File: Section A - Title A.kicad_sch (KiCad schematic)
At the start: 0 parts

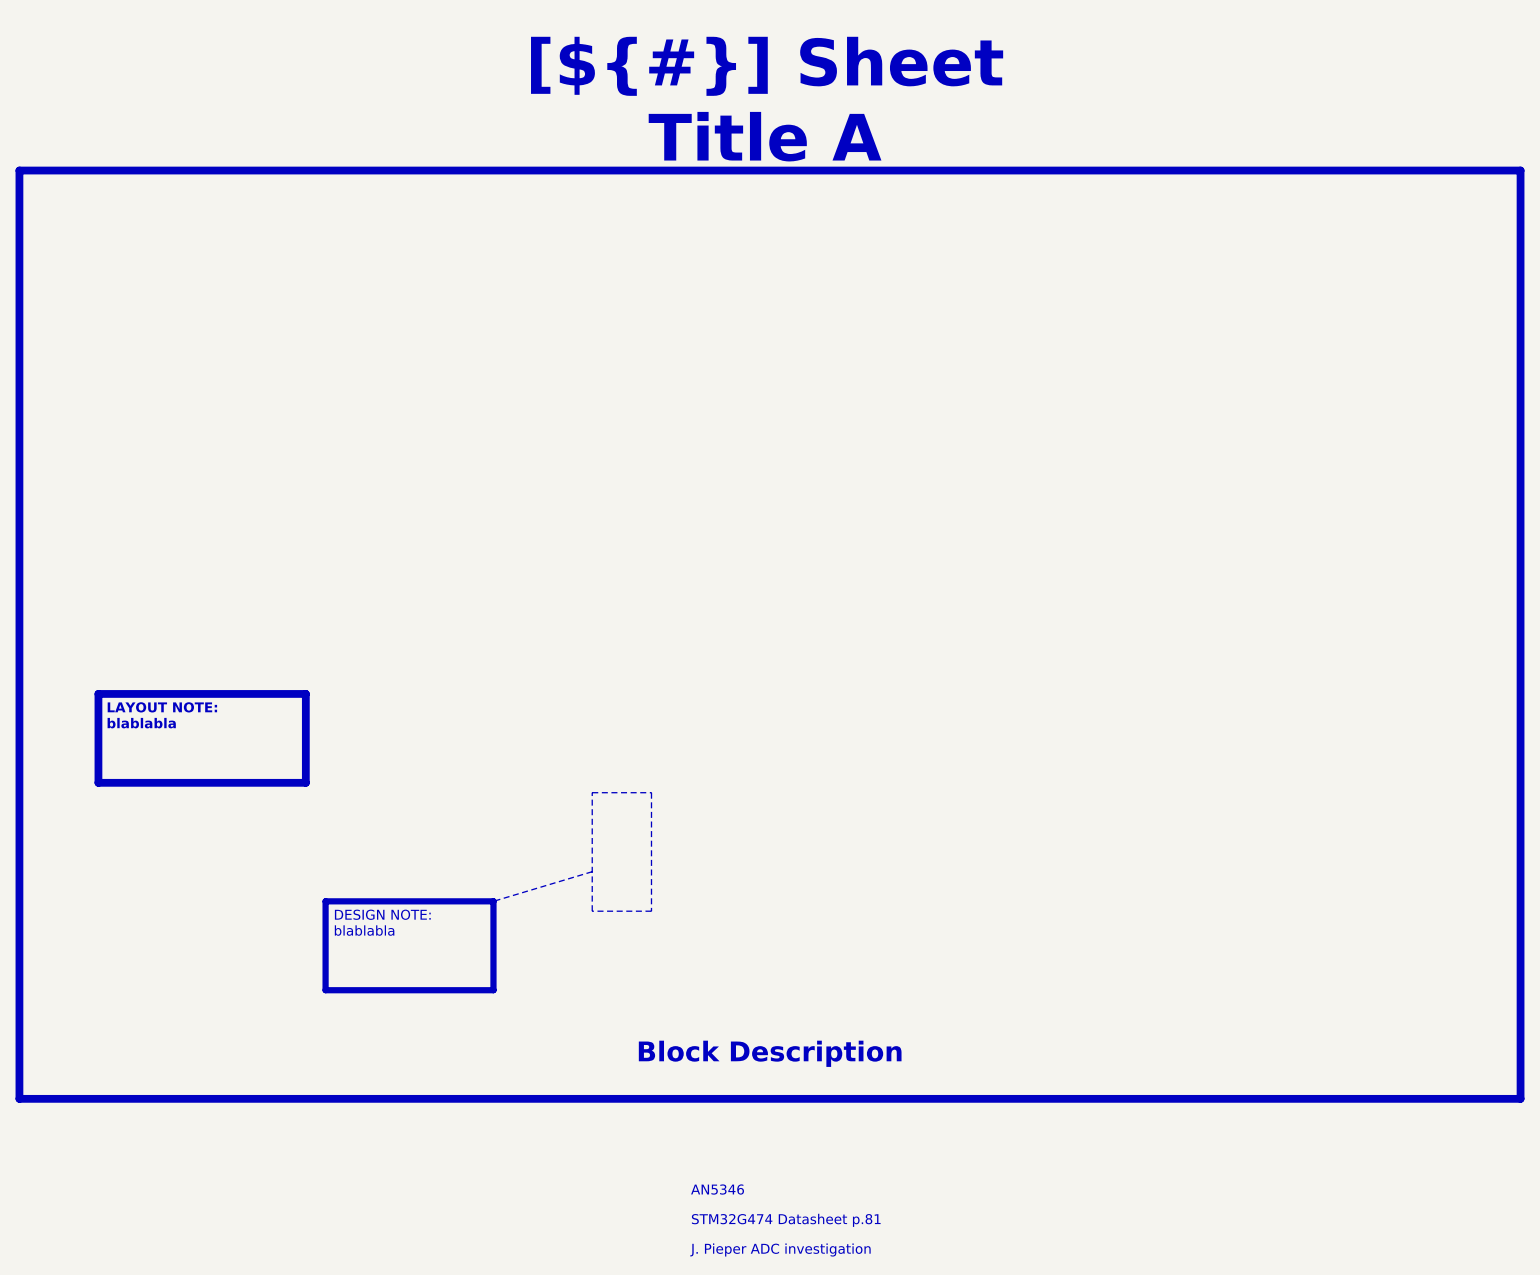
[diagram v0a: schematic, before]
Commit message: Save KiCad 10 design work
Snapshot of the schematic and PCB work done since the initial template
commit: AD7606C-18 ADC, 3x INA241A2 + PBV 1 mOhm shunts, MR60PW phase
connectors, LT8362 boost and LT3045-1 / LTC6655 analog supplies, project
libraries (lib/) and their sym/fp-lib-table.

.gitignore now excludes local history, SpinRender working files, the
stray .step export and Component Search Engine download leftovers.

Co-Authored-By: Claude Opus 5.5 <noreply@anthropic.com>
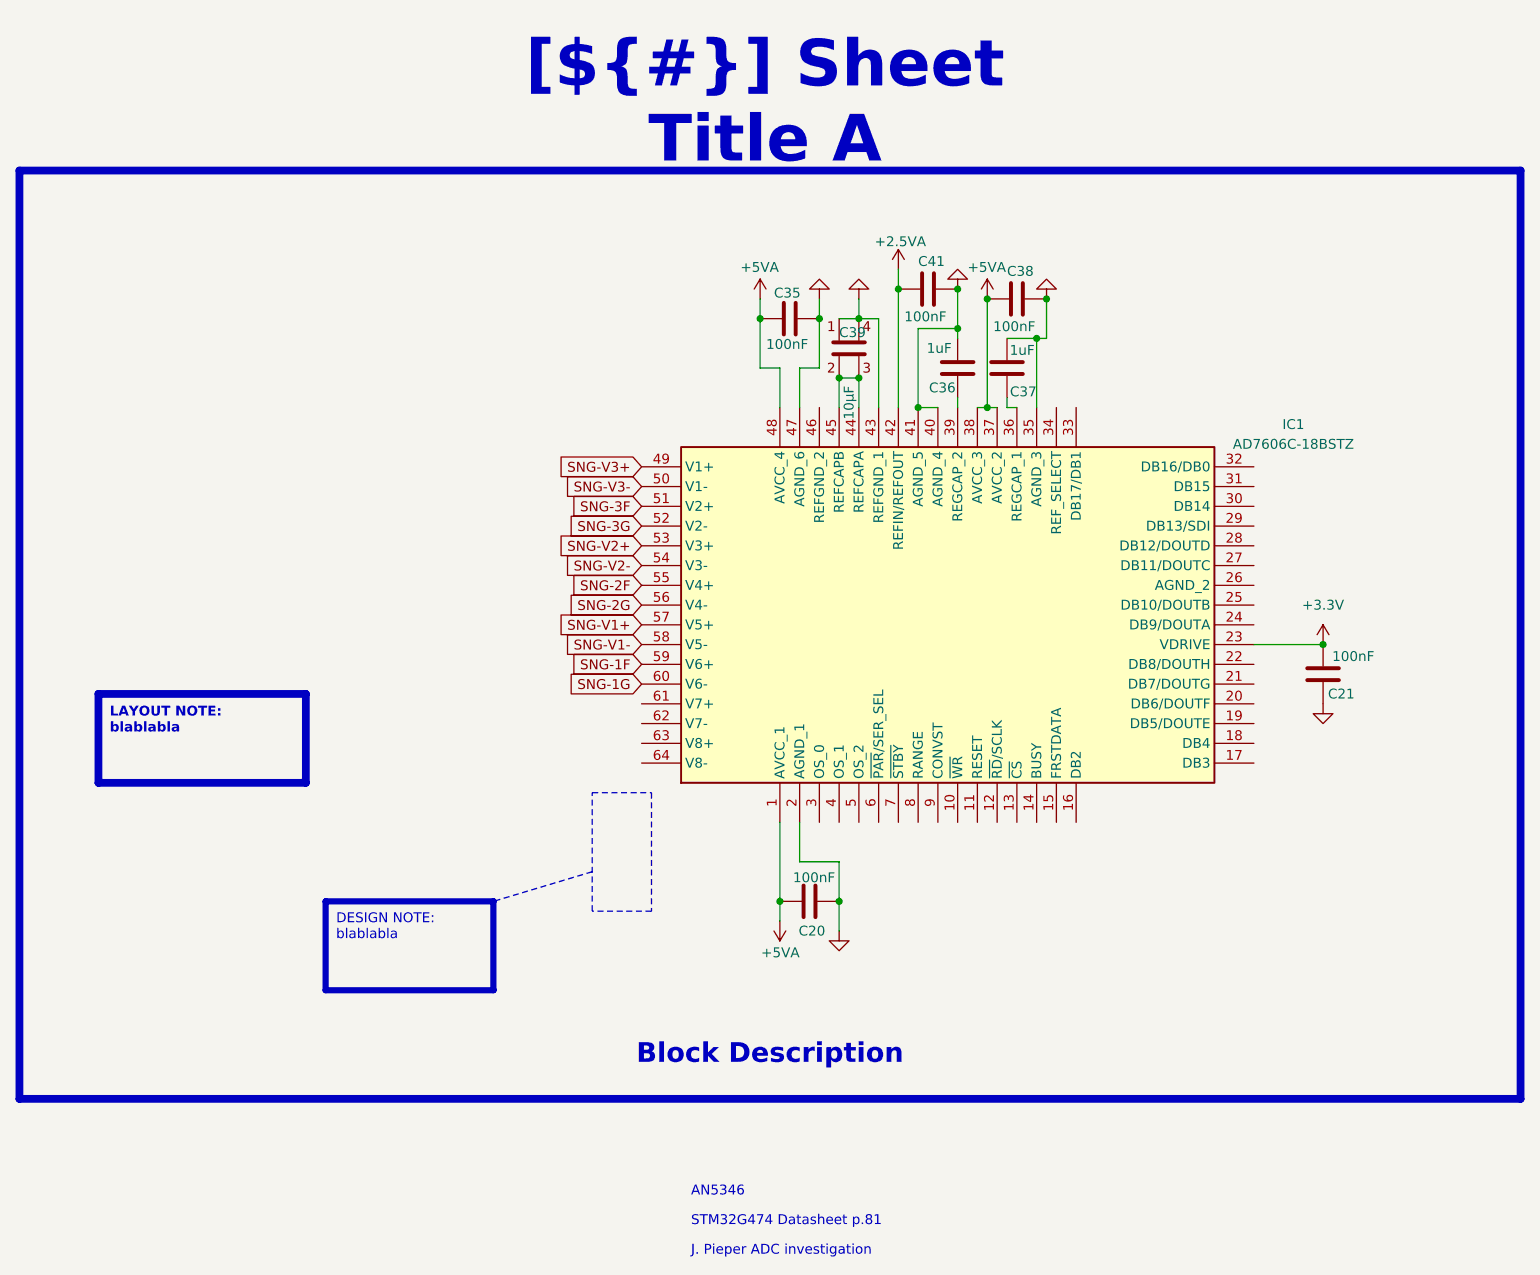
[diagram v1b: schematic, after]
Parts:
- added C20, C21, C35, C38, C41: 100nF, Capacitor_SMD:C_0603_1608Metric, symbol Device:C
- added C36, C37: 1uF, Capacitor_SMD:C_0603_1608Metric, symbol Device:C
- added C39: 10µF, Capacitor_SMD:C_0805_2012Metric, symbol Device:C
- added IC1: AD7606C-18BSTZ, QFP50P1200X1200X160-64N, symbol AD7606C-18BSTZ:AD7606C-18BSTZ
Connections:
- new net: C37.1, IC1.36 (REGCAP_1)
- new net: C36.1, IC1.39 (REGCAP_2)
- new net: C39.2, C39.3, IC1.44 (REFCAPA), IC1.45 (REFCAPB)
- new net +2.5VA: C41.2, IC1.42 (REFIN/REFOUT)
- new net +3.3V: C21.2, IC1.23 (VDRIVE)
- new net +5VA: C20.1, C35.2, C38.2, IC1.1 (AVCC_1), IC1.37 (AVCC_2), IC1.38 (AVCC_3), IC1.48 (AVCC_4)
- new net GND: C20.2, C21.1, C35.1, C36.2, C37.2, C38.1, C39.1, C39.4, C41.1, IC1.2 (AGND_1), IC1.35 (AGND_3), IC1.40 (AGND_4), IC1.41 (AGND_5), IC1.43 (REFGND_1), IC1.47 (AGND_6)
- new net SNG-1F: IC1.59 (V6+)
- new net SNG-1G: IC1.60 (V6-)
- new net SNG-2F: IC1.55 (V4+)
- new net SNG-2G: IC1.56 (V4-)
- new net SNG-3F: IC1.51 (V2+)
- new net SNG-3G: IC1.52 (V2-)
- new net SNG-V1+: IC1.57 (V5+)
- new net SNG-V1-: IC1.58 (V5-)
- new net SNG-V2+: IC1.53 (V3+)
- new net SNG-V2-: IC1.54 (V3-)
- new net SNG-V3+: IC1.49 (V1+)
- new net SNG-V3-: IC1.50 (V1-)
